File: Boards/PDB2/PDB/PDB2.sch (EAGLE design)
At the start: 24 parts, among them U1 BQ7692006PWRPW20-M, U2 STD20NF06LDPAK-M, U3 STD20NF06LDPAK-M

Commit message: yeet that lib
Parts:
- added C5: 10uF, pie:CAP0603-CAP
- added C6: .1uF, pie:CAP0603-CAP
- added C7: 1000pF, pie:CAP0603-CAP
- added C8: 22uF, pie:CAP0603-CAP
- added L1: 2.2uH, pie:ASPI-0530_INDUCTOR
- added M1: STD20NF06LDPAK-M, pie:STD20NF06LDPAK-M
- U2: value STD20NF06LDPAK-M -> Value; device pie:STD20NF06LDPAK-M -> pie:TPS62133RGTR
- renumbered U3 to M2
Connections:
- net 3_3V renamed 3.3V
- net ALERT renamed N$2
- removed net BAT+: D1.A, R5.2
- removed net VOUT-: M2.2, U2.2
- new net 12V: C5.2, C6.2, CONN1.OUTA, CONN2.OUTB, D1.A, R5.2, U$1.12V, U2.AVIN, U2.EN, U2.PVIN, U2.PVIN_2
- new net 5V: C8.2, JP2.P$1, JP3.P$1, JP4.P$1, JP5.P$1, L1.2
- new net GND_OUT: C5.1, C6.1, C7.1, C8.1, CONN1.OUTB, CONN2.OUTA, JP2.P$2, JP3.P$2, JP4.P$2, JP5.P$2, M1.2, M2.2, U2.AGND, U2.DEF, U2.EP, U2.FB, U2.FSW, U2.PGND, U2.PGND_2
- new net N$4: L1.1, U2.SW, U2.SW_2, U2.SW_3, U2.VOS
- new net N$6: C7.2, U2.SS_TR
- net DSG: now also M1.1; no longer U2.1
- net GND: now also U$1.GND
- net SOURCE: now also M1.3; no longer U2.3

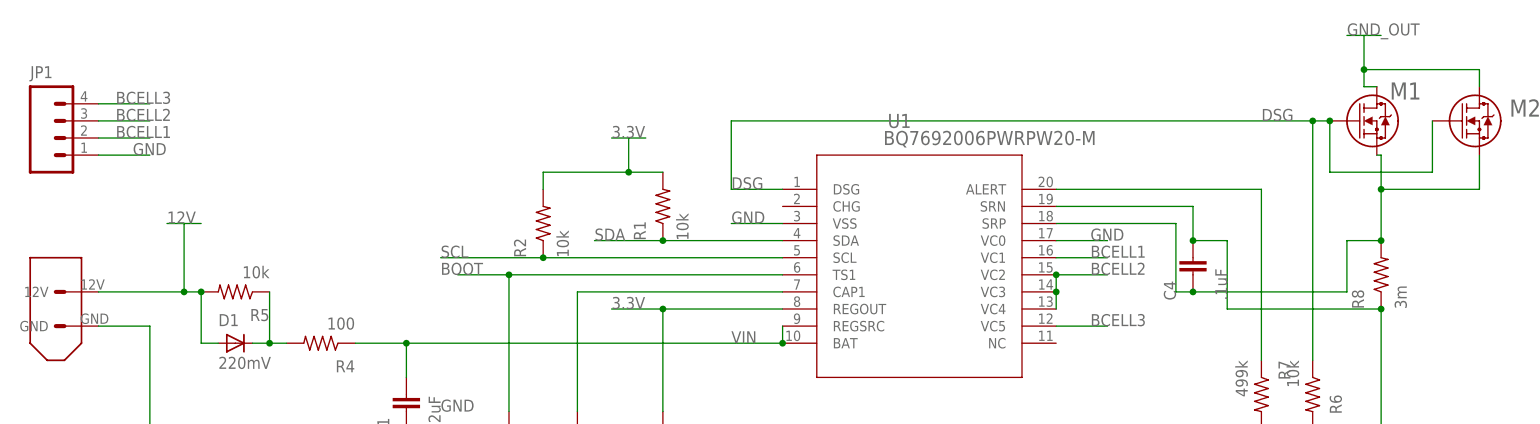
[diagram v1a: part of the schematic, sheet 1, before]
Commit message: pdb layout and added parts to library
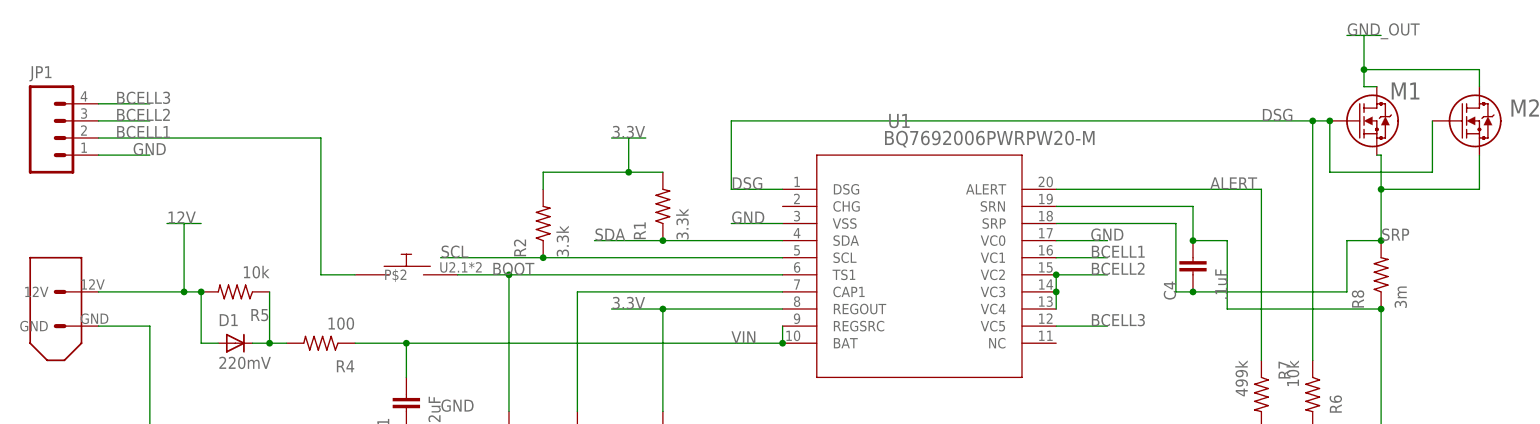
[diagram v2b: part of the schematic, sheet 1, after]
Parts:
- added C10, C9: 18pF, pie:CAP0603-CAP
- added C11: 1uF, pie:CAP0603-CAP
- added J1: AVR_SPI_PROG_5X2LOCK, SparkFun-Connectors:AVR_SPI_PROG_5X2LOCK
- added J2: (no value), SparkFun-Connectors:CONN_05X2NO_SILK
- added JP6: (no value), pie:M03PTH
- added R10, R11, R12, R13, R14, R15, R16, R17, R18, R19: 220, pie:R-US_R0603
- added R9: 10k, pie:R-US_R0603
- added U$2: D6C90F1LFS, pie:D6C90F1LFS
- added U$3: BAR_SEGMENT_DISPLAY, pie:BAR_SEGMENT_DISPLAY
- added U3: (no value), pie:ATMEGA328PB-AU
- added Y1: (no value), pie:CRYSTALSMD
- R1, R2: value 10k -> 3.3k
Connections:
- net SOURCE renamed SRP
- removed net N$2: R7.1, U1.ALERT
- new net 5V_PROG: J1.VCC, JP6.1
- new net ALERT: J2.6, R7.1, U1.ALERT
- new net BOOT_IN: J2.7, U3.(OC2B/INT1/PTCXY)PD3
- new net LED1: R10.1, U3.(OC0B/T1/PTCXY)PD5
- new net LED10: R19.1, U3.PC2(ADC2/PTCY)
- new net LED2: R11.1, U3.(OC0A/PTCXY/AIN0)PD6
- new net LED3: R12.1, U3.(PTCXY/AIN1)PD7
- new net LED4: R13.1, U3.(ICP1/CLKO/PTCXY)PB0
- new net LED5: R14.1, U3.OC1A/PTCXY)PB1
- new net LED6: R15.1, U3.(SS0/OC1B/PTCXY)PB2
- new net LED7: R16.1, U3.PE3(ADC7/PTCY/T3/MOSI1)
- new net LED8: R17.1, U3.PC0(ADC0/PTCY/MISO1)
- new net LED9: R18.1, U3.PC1(ADC1/PTCY/SCK1)
- new net MISO: J1.MISO, U3.(MISO0/RXD1/PTCXY)PB4
- new net MOSI: J1.MOSI, U3.MOSI0/TXD1/OC2A/PTCXY)PB3
- new net N$10: J1.GND@1, J1.GND@2, J1.GND@3, J1.GND@4
- new net N$11: J2.5, U3.PD2(PTCXY/INT0/OC3B/OC4B)
- new net N$12: R10.2, U$3.P1
- new net N$13: R11.2, U$3.P2
- new net N$14: R12.2, U$3.P3
- new net N$15: R13.2, U$3.P4
- new net N$16: R14.2, U$3.P5
- new net N$17: R15.2, U$3.P6
- new net N$18: R16.2, U$3.P7
- new net N$19: R17.2, U$3.P8
- new net N$20: R18.2, U$3.P9
- new net N$21: R19.2, U$3.P10
- new net N$5: C9.1, U3.(XTAL1/TOSC1)PB6, Y1.1
- new net N$7: C10.1, U3.(XTAL2/TOSC2)PB7, Y1.2
- new net N$8: J2.1, U3.PC5(ADC5/PTCY/SCL0)
- new net N$9: J2.3, U3.PC4(ADC4/PTCY/SDA0)
- new net RST: J1.RESET, R9.1, U3.PC6(RESET)
- new net SCK: J1.SCK, U3.PB5(PTCXY/XCK1/SCK0)
- new net VCC: C11.1, JP6.2, R9.2, U3.AREF, U3.AVCC, U3.VCC
- net 3.3V: now also JP6.3
- net BCELL1: now also U$2.P$1
- net BOOT: now also J2.8, U$2.P$2
- net GND: now also C10.2, C11.2, C9.2, J2.10, J2.9, U$3.P11, U$3.P12, U$3.P13, U$3.P14, U$3.P15, U$3.P16, U$3.P17, U$3.P18, U$3.P19, U$3.P20, U3.GND1, U3.GND2
- net SCL: now also J2.2
- net SDA: now also J2.4

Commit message: finished rev1 pdb:
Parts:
- removed JP1: (no value), pie:M041X04-MTA
- removed U$1: XT60CONNECTOR, pie:XT60CONNECTOR
- added J10: AVR_SPI_PROG_5X2LOCK, SparkFun-Connectors:AVR_SPI_PROG_5X2LOCK
- added J11: (no value), SparkFun-Connectors:CONN_05X2NO_SILK
- J1: value AVR_SPI_PROG_5X2LOCK -> XT60CONNECTOR; device SparkFun-Connectors:AVR_SPI_PROG_5X2LOCK -> pie:XT60CONNECTOR
- J2: device SparkFun-Connectors:CONN_05X2NO_SILK -> pie:M041X04-MTA
- renumbered CONN1 to J4, CONN2 to J3, JP2 to J5, JP3 to J6, JP4 to J7, JP5 to J8, JP6 to J9, U$2 to BUT1, U$3 to LED1
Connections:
- removed net N$10: J1.GND@1, J1.GND@2, J1.GND@3, J1.GND@4
- removed net N$9: J2.3, U3.PC4(ADC4/PTCY/SDA0)
- new net N$2: J11.1, U3.PC4(ADC4/PTCY/SDA0)
- net 12V: now also J1.12V; no longer U$1.12V
- net 5V_PROG: now also J10.VCC; no longer J1.VCC
- net ALERT: now also J11.8; no longer J2.6
- net BCELL1: now also J2.2; no longer JP1.2
- net BCELL2: now also J2.3; no longer JP1.3
- net BCELL3: now also J2.4; no longer JP1.4
- net BOOT: now also J11.6; no longer J2.8
- net BOOT_IN: now also J11.5; no longer J2.7
- net GND: now also J1.GND, J10.GND@1, J10.GND@2, J10.GND@3, J10.GND@4, J11.10, J11.9, J2.1; no longer J2.10, J2.9, JP1.1, U$1.GND
- net MISO: now also J10.MISO; no longer J1.MISO
- net MOSI: now also J10.MOSI; no longer J1.MOSI
- net N$11: now also J11.7; no longer J2.5
- net N$8: now also J11.3; no longer J2.1
- net RST: now also J10.RESET; no longer J1.RESET
- net SCK: now also J10.SCK; no longer J1.SCK
- net SCL: now also J11.4; no longer J2.2
- net SDA: now also J11.2; no longer J2.4

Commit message: yeet
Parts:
- removed R4: 100, pie:R-US_R0603
- added J12: (no value), SparkFun-Connectors:CONN_02
- added R20: 100k, pie:R-US_R0603
- C5, C8: device pie:CAP0603-CAP -> pie:CAP0805
- R6: value 10k -> 5.6k
- R8: value 3m -> 5m; device pie:R-US_R2512 -> pie:SHUNT_SMD; MANUFACTURER_PART_NO (none) -> WSHM28185L000FEA
- Y1: device pie:CRYSTALSMD -> pie:ECX-53BSMDCRYSTAL; PARTNO ABLS-8.000MHZ-B4-T -> (none)
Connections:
- removed net N$3: D1.C, R4.2, R5.1
- new net PG: R20.1, U2.PG, U3.PC3(ADC3/PTCY)
- new net RXD: J12.1, U3.PD0(PTCXY/OC3A/RXD0)
- new net TXD: J12.2, U3.PD1(PTCXY/OC4A/TXD0)
- net 5V: now also R20.2, U2.FSW, U2.VOS
- net DSG: now also R6.2; no longer R6.1
- net GND: now also R6.1, Y1G$2.GND; no longer R6.2
- net GND_OUT: no longer U2.FSW
- net N$4: no longer U2.VOS
- net N$5: now also Y1G$1.2; no longer Y1.1
- net N$7: now also Y1G$1.1; no longer Y1.2
- net VIN: now also D1.C, R5.1; no longer R4.1
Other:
- moved on the sheet: R6, Y1G$1
